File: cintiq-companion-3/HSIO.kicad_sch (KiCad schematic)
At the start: 9 parts, among them J3 Bus_M.2_Socket_M

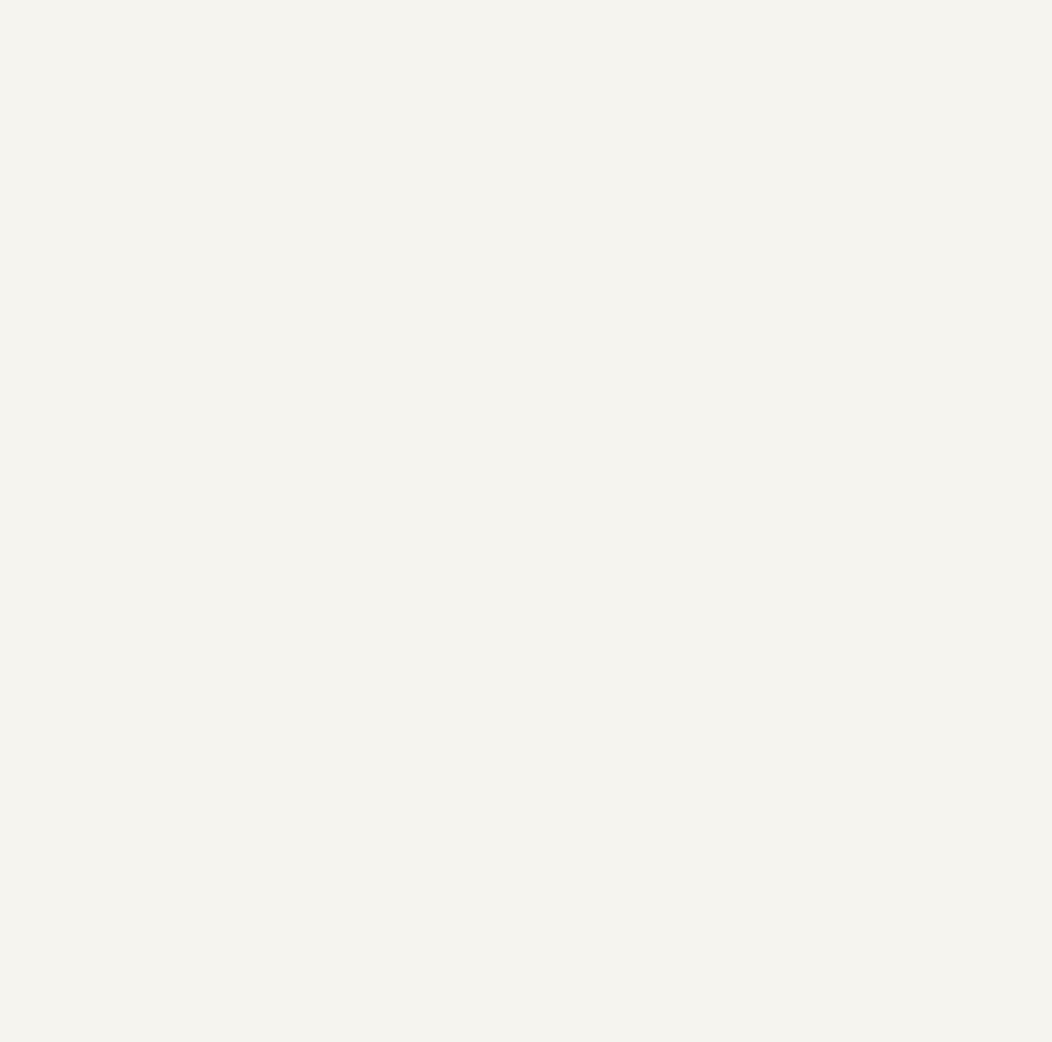
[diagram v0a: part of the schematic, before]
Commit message: Added E-key slot
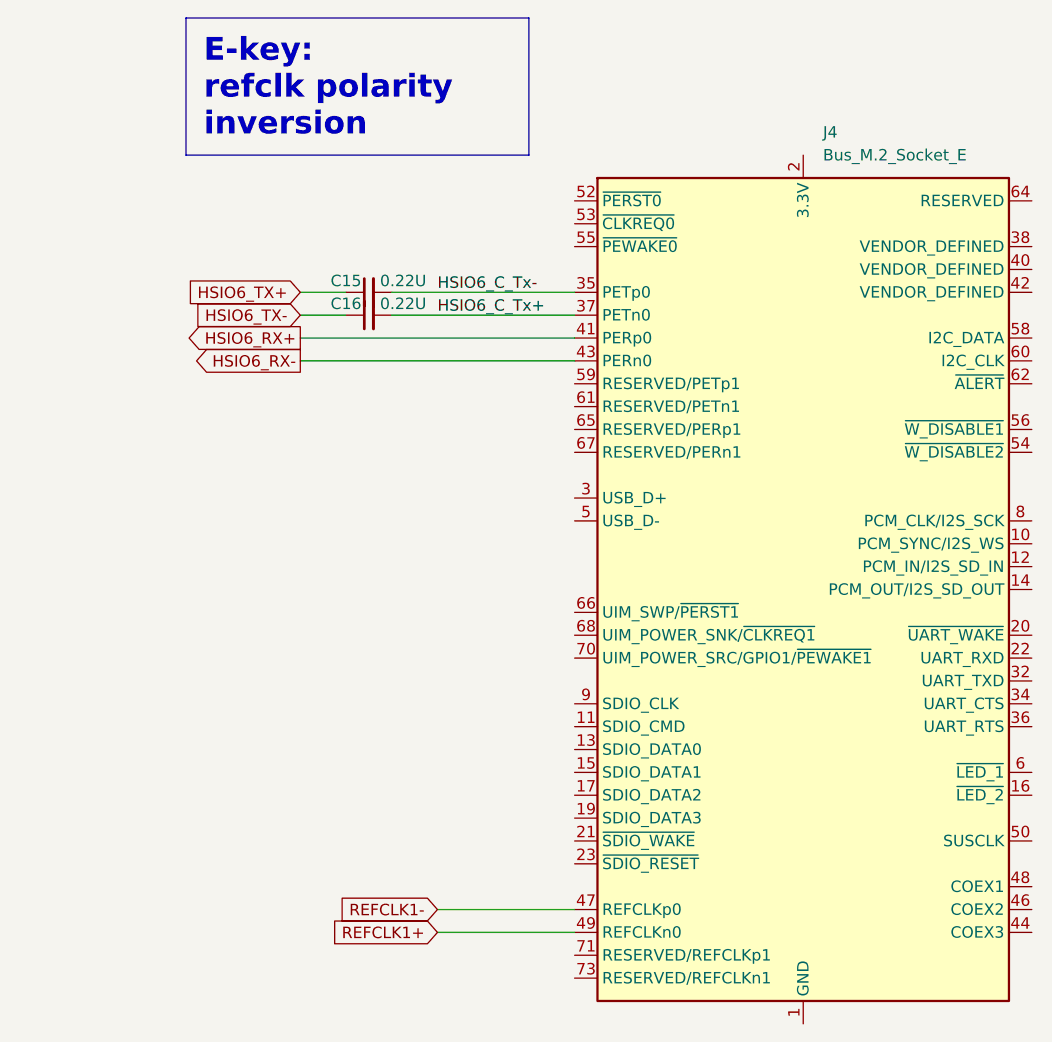
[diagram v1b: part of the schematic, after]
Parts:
- added C15, C16: 0.22U, Capacitor_SMD:C_0402_1005Metric, symbol Device:C_Small
- added J4: Bus_M.2_Socket_E, A_my_stuff:e-key, symbol Connector:Bus_M.2_Socket_E
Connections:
- new net: J4.1 (GND), J4.18 (GND), J4.33 (GND), J4.39 (GND), J4.45 (GND), J4.51 (GND), J4.57 (GND), J4.63 (GND), J4.69 (GND), J4.7 (GND), J4.75 (GND)
- new net: J4.2 (3.3V), J4.4 (3.3V), J4.72 (3.3V), J4.74 (3.3V)
- new net HSIO6_C_Tx+: C16.2, J4.37 (PETn0)
- new net HSIO6_C_Tx-: C15.2, J4.35 (PETp0)
- new net HSIO6_RX+: J4.41 (PERp0)
- new net HSIO6_RX-: J4.43 (PERn0)
- new net HSIO6_TX+: C15.1
- new net HSIO6_TX-: C16.1
- new net REFCLK1+: J4.49 (REFCLKn0)
- new net REFCLK1-: J4.47 (REFCLKp0)

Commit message: susclk
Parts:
- added R10, R11: 0Ω, A_HDJ_Library:R_0402_1005Metric, symbol Device:R
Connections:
- net at J3.68 (SUSCLK): now also R11.1
- net at J4.50 (SUSCLK): now also R10.1
- new net SUSCLK_WIFI: R10.2, R11.2

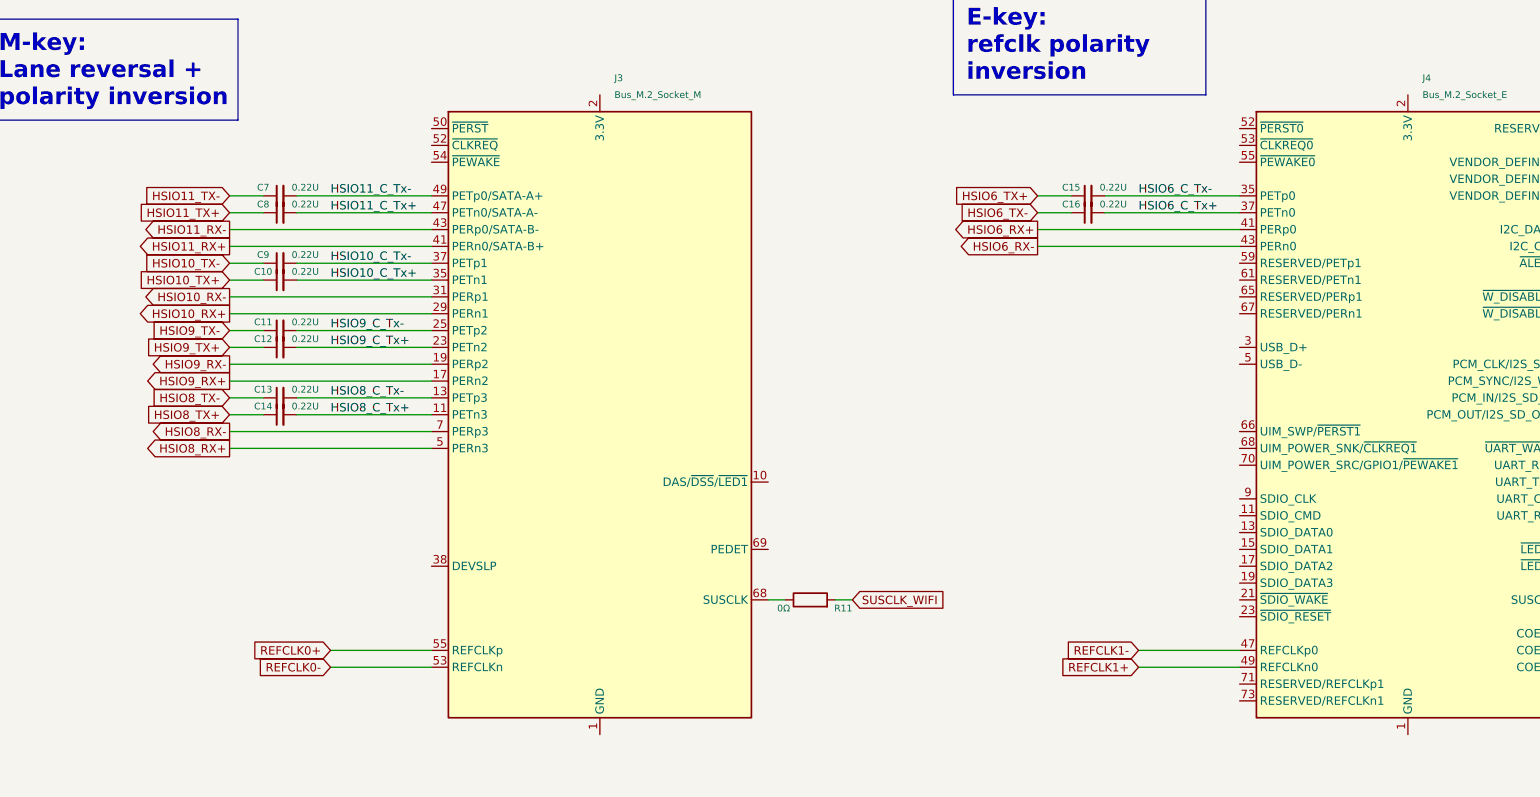
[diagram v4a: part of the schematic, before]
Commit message: renamed pcie nets
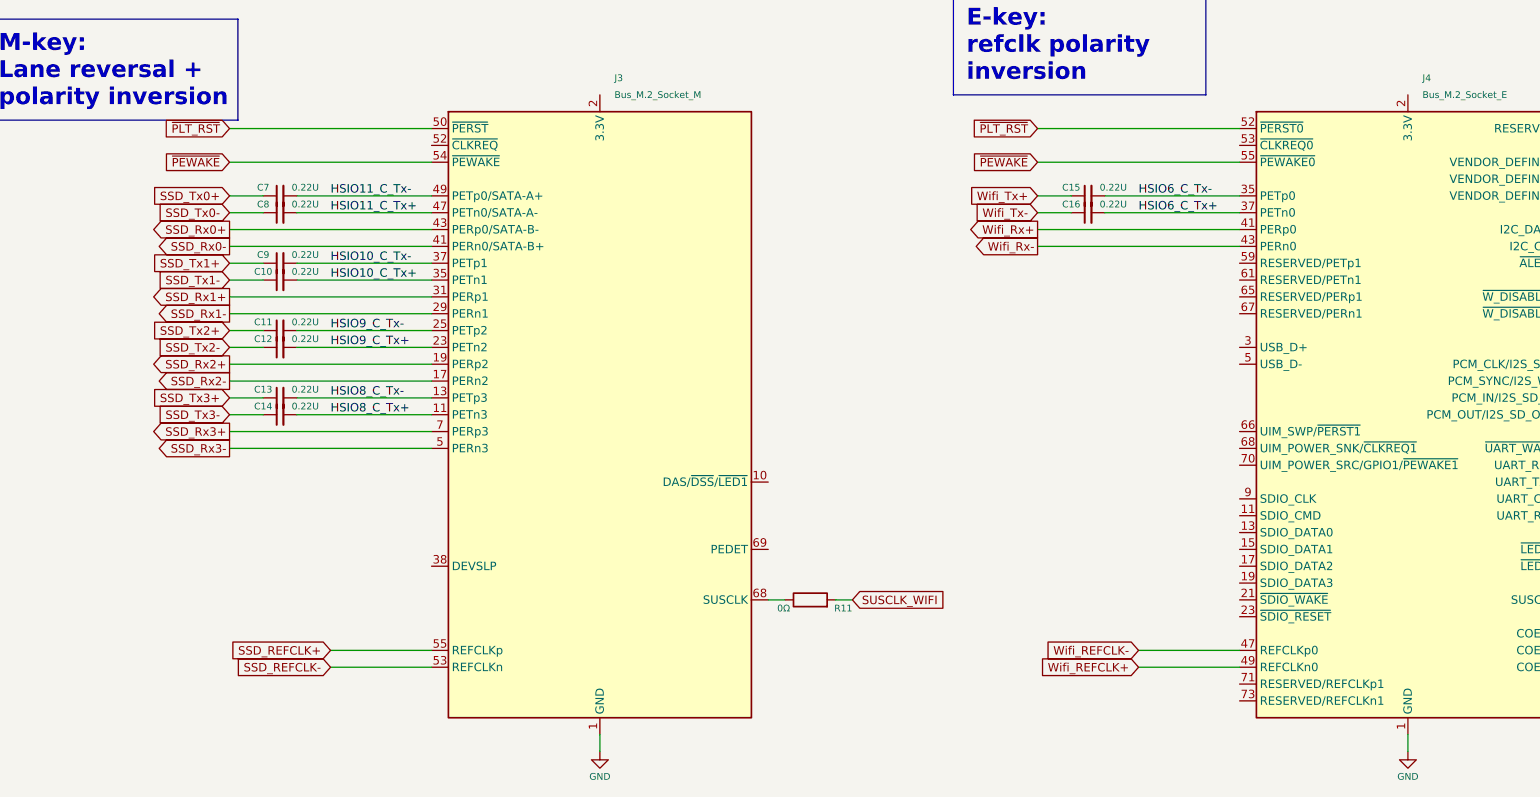
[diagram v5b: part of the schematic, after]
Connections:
- net GND: now reaches J3.1 (GND), J3.15 (GND), J3.21 (GND), J3.27 (GND), J3.3 (GND), J3.33 (GND), J3.39 (GND), J3.45 (GND), J3.51 (GND), J3.57 (GND), J3.71 (GND), J3.73 (GND), J3.75 (GND), J3.9 (GND)
- net GND: now also J4.1 (GND), J4.18 (GND), J4.33 (GND), J4.39 (GND), J4.45 (GND), J4.51 (GND), J4.57 (GND), J4.63 (GND), J4.69 (GND), J4.7 (GND), J4.75 (GND)
- net ~{PLT_RST}: now reaches J3.50 (~{PERST})
- net ~{PLT_RST}: now also J4.52 (~{PERST0})
- net ~{PEWAKE}: now reaches J3.54 (~{PEWAKE})
- net ~{PEWAKE}: now also J4.55 (~{PEWAKE0})
- net HSIO10_RX+ renamed SSD_Rx1-
- net HSIO10_RX- renamed SSD_Rx1+
- net HSIO10_TX+ renamed SSD_Tx1-
- net HSIO10_TX- renamed SSD_Tx1+
- net HSIO11_RX+ renamed SSD_Rx0-
- net HSIO11_RX- renamed SSD_Rx0+
- net HSIO11_TX+ renamed SSD_Tx0-
- net HSIO11_TX- renamed SSD_Tx0+
- net HSIO6_RX+ renamed Wifi_Rx+
- net HSIO6_RX- renamed Wifi_Rx-
- net HSIO6_TX+ renamed Wifi_Tx+
- net HSIO6_TX- renamed Wifi_Tx-
- net HSIO8_RX+ renamed SSD_Rx3-
- net HSIO8_RX- renamed SSD_Rx3+
- net HSIO8_TX+ renamed SSD_Tx3-
- net HSIO8_TX- renamed SSD_Tx3+
- net HSIO9_RX+ renamed SSD_Rx2-
- net HSIO9_RX- renamed SSD_Rx2+
- net HSIO9_TX+ renamed SSD_Tx2-
- net HSIO9_TX- renamed SSD_Tx2+
- net REFCLK0+ renamed SSD_REFCLK+
- net REFCLK0- renamed SSD_REFCLK-
- net REFCLK1+ renamed Wifi_REFCLK+
- net REFCLK1- renamed Wifi_REFCLK-

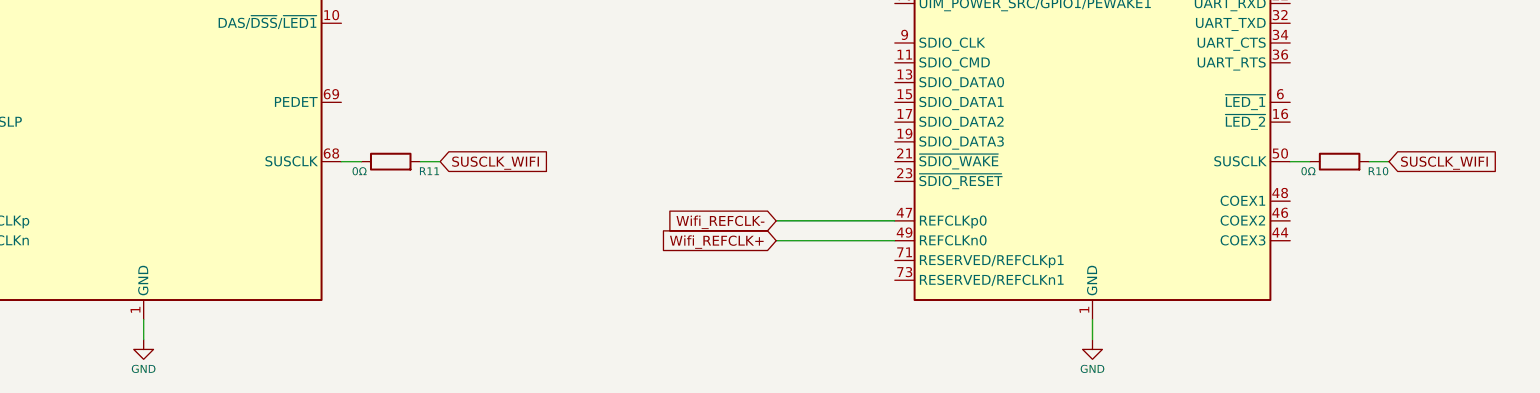
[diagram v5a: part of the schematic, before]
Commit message: routed usb
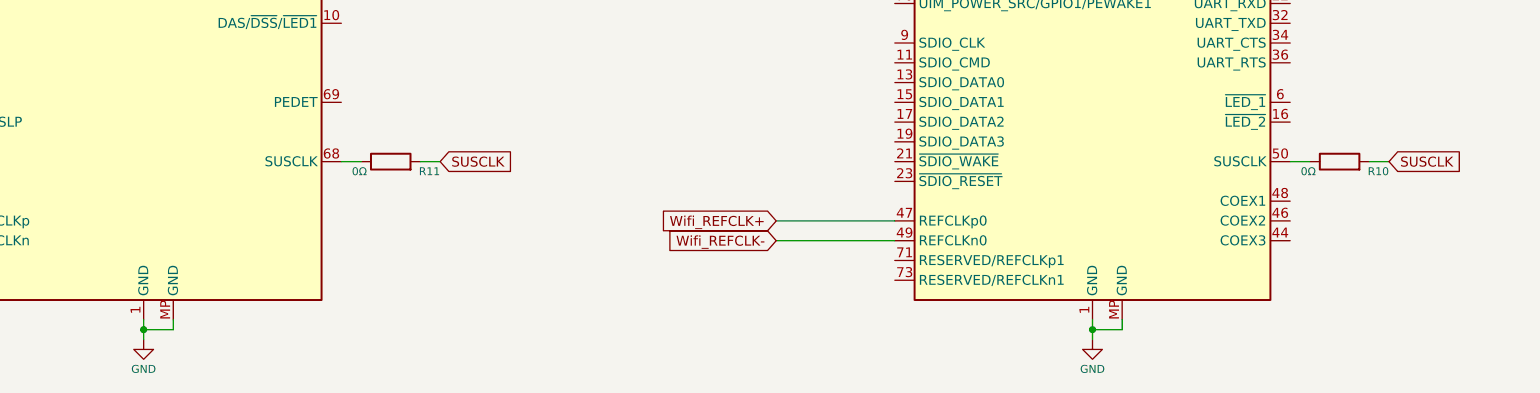
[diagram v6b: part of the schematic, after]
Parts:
- R10, R11: footprint A_HDJ_Library:R_0402_1005Metric -> Resistor_SMD:R_0402_1005Metric
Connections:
- net GND: now also J3.MP (GND), J4.MP (GND)
- net Wifi_REFCLK+: now also J4.47 (REFCLKp0); no longer J4.49 (REFCLKn0)
- net Wifi_REFCLK-: now also J4.49 (REFCLKn0); no longer J4.47 (REFCLKp0)
- net SUSCLK_WIFI renamed SUSCLK
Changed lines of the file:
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@@
 	(generator_version "8.0")
 	(paper "A4")
+	(junction
+		(at 109.22 139.7)
+		(diameter 0)
+		(color 0 0 0 0)
+	)
+	(junction
+		(at 231.14 139.7)
+		(diameter 0)
+		(color 0 0 0 0)
+	)
 	(wire
 		(pts
@@
 	(wire
 		(pts
+			(xy 231.14 139.7) (xy 234.95 139.7)
+		)
+		(stroke
+			(width 0)
+			(type default)
+		)
+	)
+	(wire
+		(pts
 			(xy 63.5 67.31) (xy 83.82 67.31)
 		)
@@
 	(wire
 		(pts
-			(xy 231.14 138.43) (xy 231.14 140.97)
+			(xy 231.14 138.43) (xy 231.14 139.7)
 		)
 		(stroke
@@
 	(wire
 		(pts
+			(xy 113.03 138.43) (xy 113.03 139.7)
+		)
+		(stroke
+			(width 0)
+			(type default)
+		)
+	)
+	(wire
+		(pts
 			(xy 205.74 59.69) (xy 185.42 59.69)
 		)
@@
 	(wire
 		(pts
+			(xy 231.14 139.7) (xy 231.14 140.97)
+		)
+		(stroke
+			(width 0)
+			(type default)
+		)
+	)
+	(wire
+		(pts
 			(xy 53.34 64.77) (xy 83.82 64.77)
 		)
@@
 	(wire
 		(pts
-			(xy 109.22 138.43) (xy 109.22 140.97)
+			(xy 109.22 139.7) (xy 109.22 140.97)
+		)
+		(stroke
+			(width 0)
+			(type default)
+		)
+	)
+	(wire
+		(pts
+			(xy 109.22 138.43) (xy 109.22 139.7)
 		)
 		(stroke
@@
 	(wire
 		(pts
+			(xy 109.22 139.7) (xy 113.03 139.7)
+		)
+		(stroke
+			(width 0)
+			(type default)
+		)
+	)
+	(wire
+		(pts
 			(xy 63.5 59.69) (xy 83.82 59.69)
 		)
@@
 		(pts
 			(xy 58.42 77.47) (xy 53.34 77.47)
+		)
+		(stroke
+			(width 0)
+			(type default)
+		)
+	)
+	(wire
+		(pts
+			(xy 234.95 138.43) (xy 234.95 139.7)
 		)
 		(stroke
@@
 	(global_label "Wifi_REFCLK+"
 		(shape input)
-		(at 190.5 128.27 180)
-		(fields_autoplaced yes)
-		(effects
-			(font
-				(size 1.27 1.27)
-			)
-			(justify right)
-		)
-		(property "Intersheetrefs" "${INTERSHEET_REFS}"
-			(at 174.5124 128.27 0)
+		(at 190.5 125.73 180)
+		(fields_autoplaced yes)
+		(effects
+			(font
+				(size 1.27 1.27)
+			)
+			(justify right)
+		)
+		(property "Intersheetrefs" "${INTERSHEET_REFS}"
+			(at 174.5124 125.73 0)
 			(effects
 				(font
@@
 		)
 	)
-	(global_label "SUSCLK_WIFI"
+	(global_label "SUSCLK"
 		(shape input)
 		(at 147.32 118.11 0)
@@
 		)
 		(property "Intersheetrefs" "${INTERSHEET_REFS}"
-			(at 147.32 118.11 0)
-			(effects
-				(font
-					(size 1.27 1.27)
-				)
+			(at 157.6228 118.11 0)
+			(effects
+				(font
+					(size 1.27 1.27)
+				)
+				(justify left)
 				(hide yes)
 			)
@@
 	(global_label "Wifi_REFCLK-"
 		(shape input)
-		(at 190.5 125.73 180)
-		(fields_autoplaced yes)
-		(effects
-			(font
-				(size 1.27 1.27)
-			)
-			(justify right)
-		)
-		(property "Intersheetrefs" "${INTERSHEET_REFS}"
-			(at 174.5124 125.73 0)
-			(effects
-				(font
-					(size 1.27 1.27)
-				)
-				(justify right)
-				(hide yes)
-			)
-		)
-	)
-	(global_label "SUSCLK_WIFI"
+		(at 190.5 128.27 180)
+		(fields_autoplaced yes)
+		(effects
+			(font
+				(size 1.27 1.27)
+			)
+			(justify right)
+		)
+		(property "Intersheetrefs" "${INTERSHEET_REFS}"
+			(at 174.5124 128.27 0)
+			(effects
+				(font
+					(size 1.27 1.27)
+				)
+				(justify right)
+				(hide yes)
+			)
+		)
+	)
+	(global_label "SUSCLK"
 		(shape input)
 		(at 269.24 118.11 0)
@@
 		)
 		(property "Intersheetrefs" "${INTERSHEET_REFS}"
-			(at 269.24 118.11 0)
-			(effects
-				(font
-					(size 1.27 1.27)
-				)
+			(at 279.5428 118.11 0)
+			(effects
+				(font
+					(size 1.27 1.27)
+				)
+				(justify left)
 				(hide yes)
 			)
@@
 			)
 		)
-		(property "Footprint" "A_HDJ_Library:R_0402_1005Metric"
+		(property "Footprint" "Resistor_SMD:R_0402_1005Metric"
 			(at 140.97 119.888 90)
 			(effects
@@
 			)
 		)
-		(property "Footprint" "A_HDJ_Library:R_0402_1005Metric"
+		(property "Footprint" "Resistor_SMD:R_0402_1005Metric"
 			(at 262.89 119.888 90)
 			(effects
@@
 		(pin "75"
 		)
+		(pin "MP"
+		)
 		(instances
 			(project "cintiq-companion-3"
@@
 		(pin "8"
 		)
+		(pin "MP"
+		)
 		(instances
